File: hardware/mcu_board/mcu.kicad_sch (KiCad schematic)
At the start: 18 parts, among them J1 COLD, J1 TANK-BOTTOM, J1 TANK-TOP, J4 DISPLAY, J6 Conn_01x02_Pin, J7 RTC, SW1 RotaryEncoder_Switch, U1 ESP32-S3-DevKitC, U2 TOP, U3 BOTTOM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

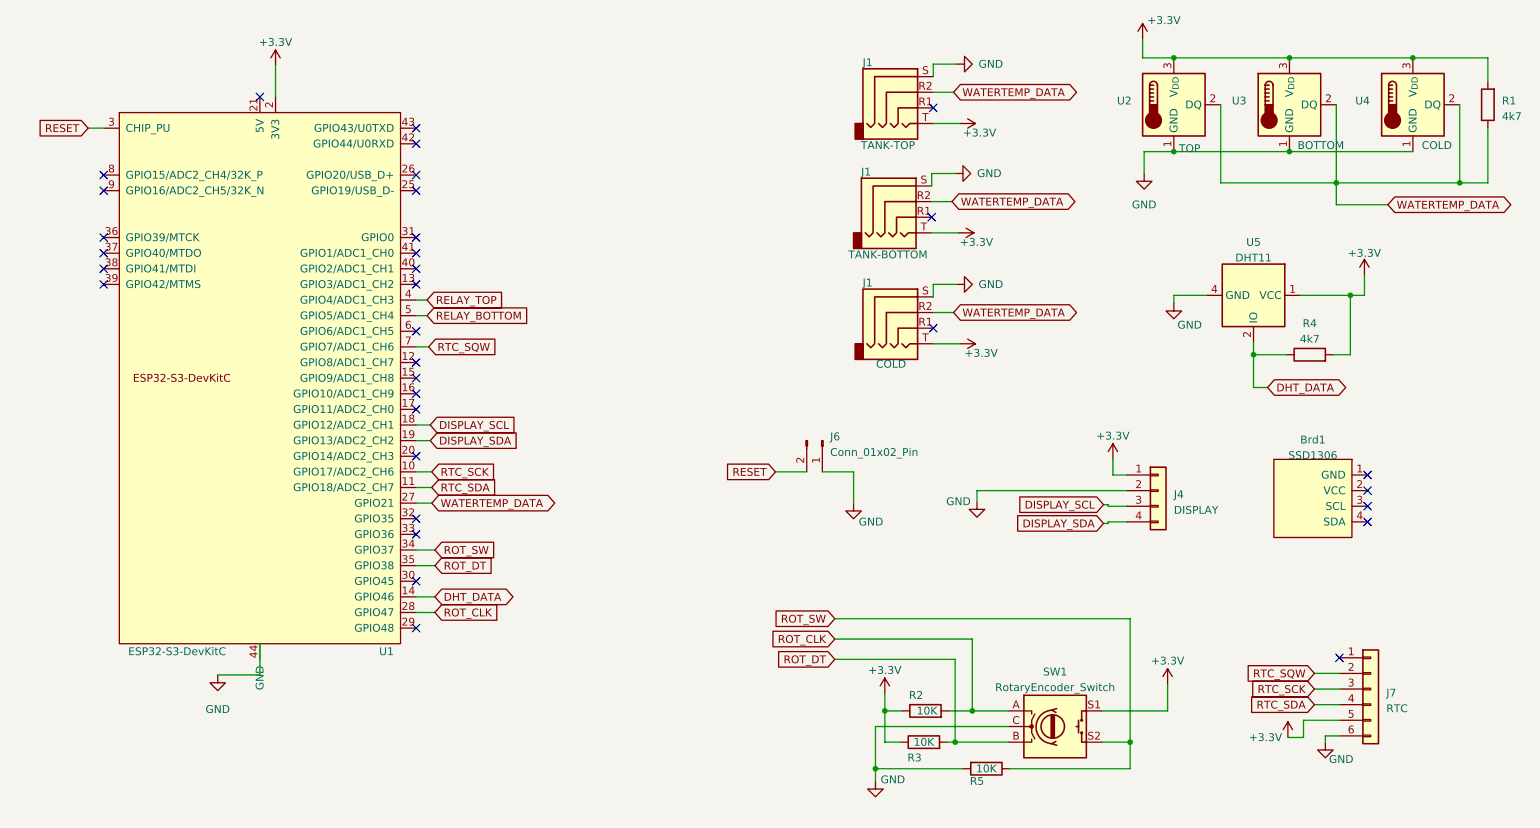
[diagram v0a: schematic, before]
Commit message: Refactored PCBs for v2. See README
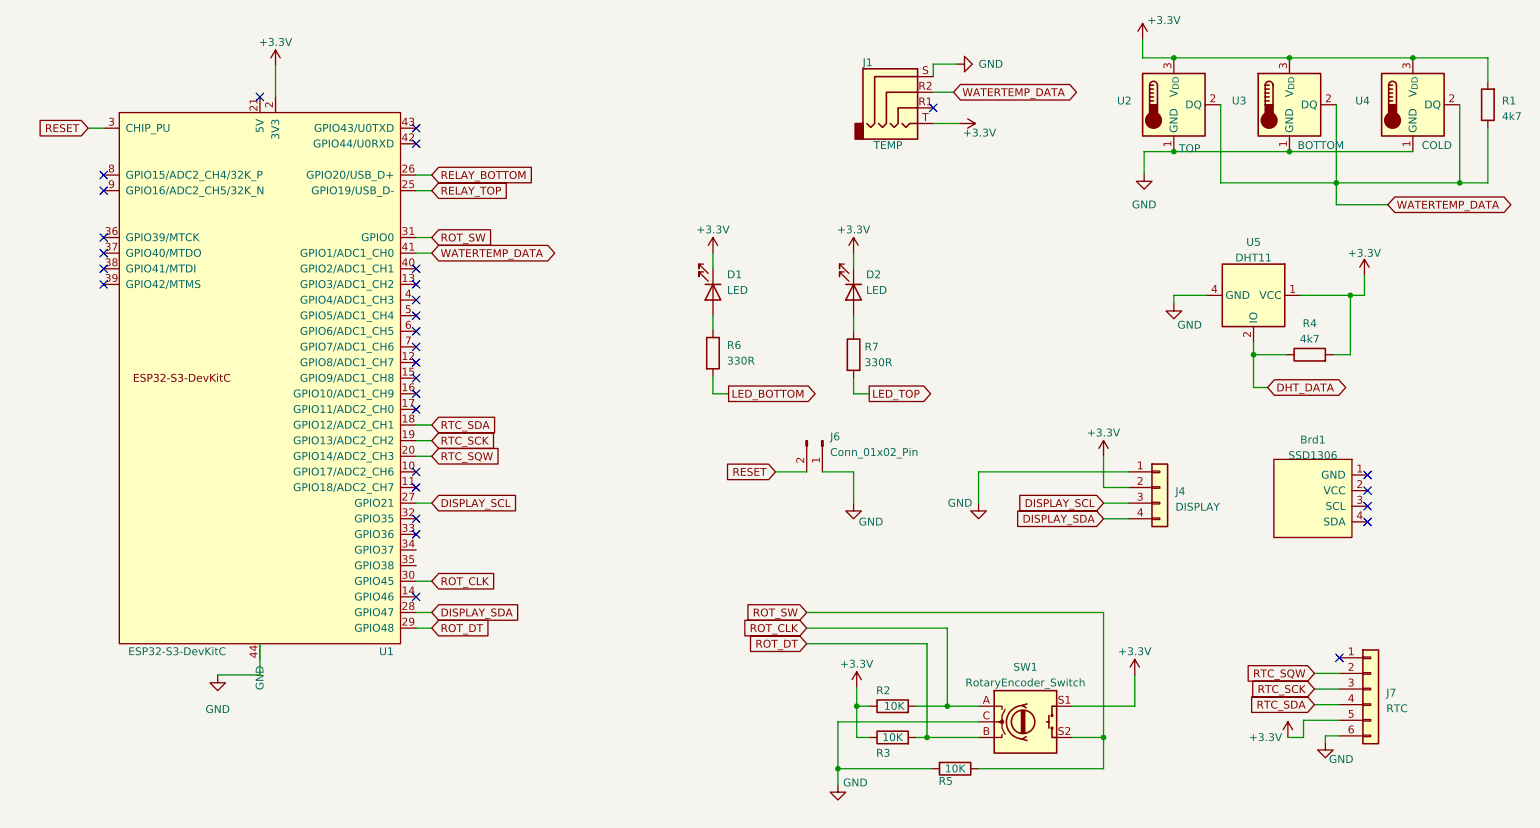
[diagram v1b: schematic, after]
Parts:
- removed J1: TANK-BOTTOM, Connector_Audio:Jack_3.5mm_PJ320D_Horizontal_NG, symbol Connector_Audio:AudioJack4
- removed J1: COLD, Connector_Audio:Jack_3.5mm_PJ320D_Horizontal_NG, symbol Connector_Audio:AudioJack4
- added D1, D2: LED, Diode_SMD:D_0805_2012Metric_Pad1.15x1.40mm_HandSolder, symbol Device:LED
- added R6, R7: 330R, Resistor_SMD:R_0805_2012Metric_Pad1.20x1.40mm_HandSolder, symbol Device:R
- J1: value TANK-TOP -> TEMP
- R4, U5: now left out of the parts list
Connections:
- net +3.3V: now also J4.2 (Pin_2), D1.1 (K), D2.1 (K); no longer J4.1 (Pin_1)
- net DHT_DATA: no longer U1.14 (GPIO46)
- net DISPLAY_SCL: now also U1.27 (GPIO21); no longer U1.18 (GPIO12/ADC2_CH1)
- net DISPLAY_SDA: now also U1.28 (GPIO47); no longer U1.19 (GPIO13/ADC2_CH2)
- net GND: now also J4.1 (Pin_1); no longer J4.2 (Pin_2)
- net RELAY_BOTTOM: now also U1.26 (GPIO20/USB_D+); no longer U1.5 (GPIO5/ADC1_CH4)
- net RELAY_TOP: now also U1.25 (GPIO19/USB_D-); no longer U1.4 (GPIO4/ADC1_CH3)
- net ROT_CLK: now also U1.30 (GPIO45); no longer U1.28 (GPIO47)
- net ROT_DT: now also U1.29 (GPIO48); no longer U1.35 (GPIO38)
- net ROT_SW: now also U1.31 (GPIO0); no longer U1.34 (GPIO37)
- net RTC_SCK: now also U1.19 (GPIO13/ADC2_CH2); no longer U1.10 (GPIO17/ADC2_CH6)
- net RTC_SDA: now also U1.18 (GPIO12/ADC2_CH1); no longer U1.11 (GPIO18/ADC2_CH7)
- net RTC_SQW: now also U1.20 (GPIO14/ADC2_CH3); no longer U1.7 (GPIO7/ADC1_CH6)
- net WATERTEMP_DATA: now also U1.41 (GPIO1/ADC1_CH0); no longer U1.27 (GPIO21)
- new net: D1.2 (A), R6.1
- new net: D2.2 (A), R7.1
- new net LED_BOTTOM: R6.2
- new net LED_TOP: R7.2
- no-connect marks 33 -> 30
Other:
- moved on the sheet: J4, R2, R3, R5, SW1

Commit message: v2 layout changes to fit in bax
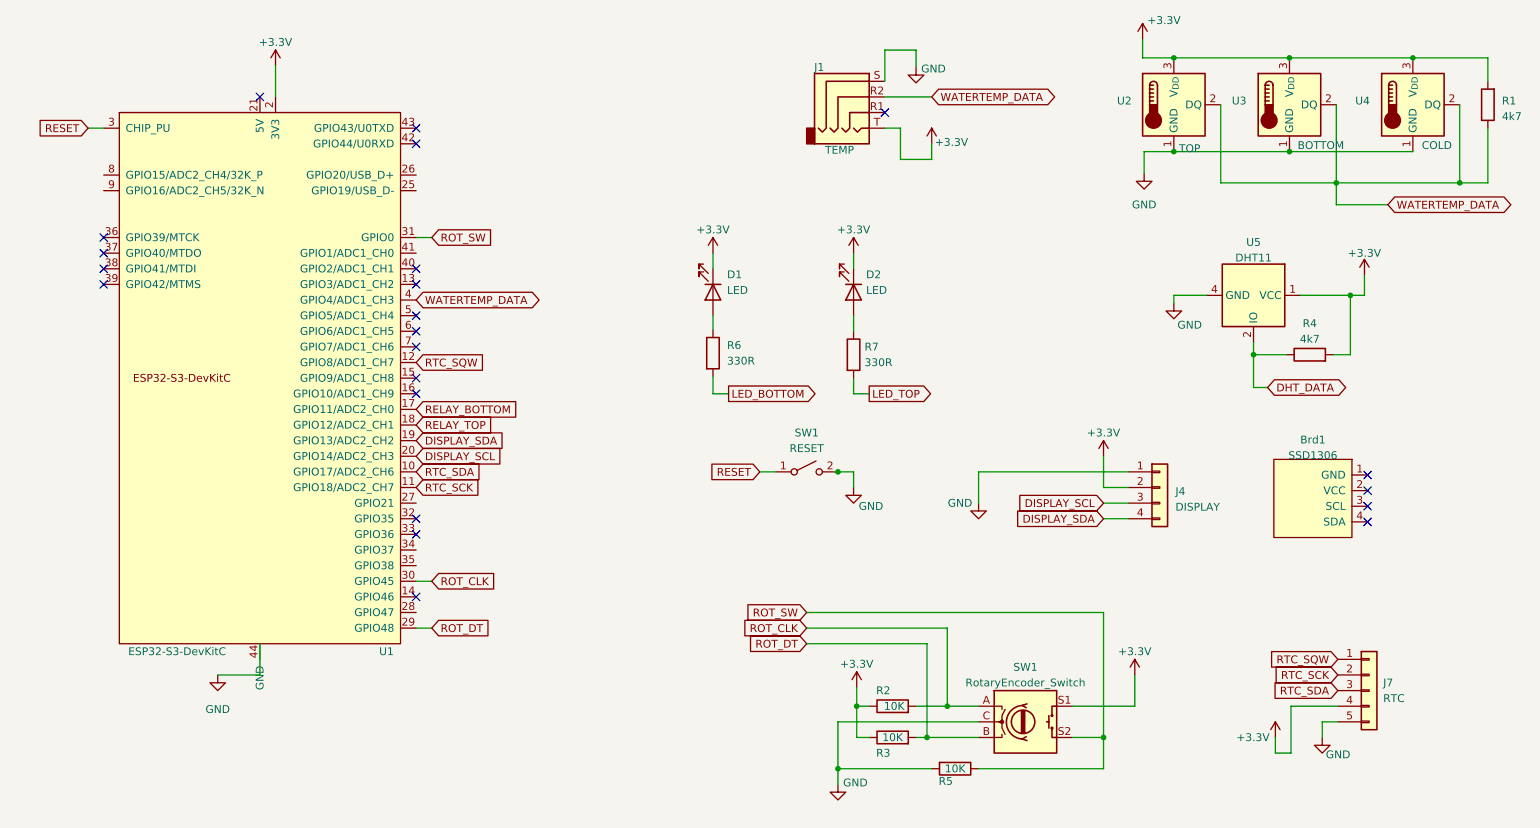
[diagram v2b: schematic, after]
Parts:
- removed J6: Conn_01x02_Pin, Connector_PinHeader_2.54mm:PinHeader_1x02_P2.54mm_Vertical, symbol Connector:Conn_01x02_Pin
- added SW1: RESET, Button_Switch_THT:SW_Tactile_SPST_Angled_PTS645Vx39-2LFS, symbol Switch:SW_SPST
- J7: footprint Connector_PinHeader_2.54mm:PinHeader_1x06_P2.54mm_Vertical -> Connector_PinHeader_2.54mm:PinHeader_1x05_P2.54mm_Vertical; symbol Connector_Generic:Conn_01x06 -> Connector_Generic:Conn_01x05
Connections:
- net +3.3V: now also J7.4 (Pin_4); no longer J7.5 (Pin_5)
- net DISPLAY_SCL: now also U1.20 (GPIO14/ADC2_CH3); no longer U1.27 (GPIO21)
- net DISPLAY_SDA: now also U1.19 (GPIO13/ADC2_CH2); no longer U1.28 (GPIO47)
- net GND: now also J7.5 (Pin_5), SW1.2 (B); no longer J7.6 (Pin_6)
- net RELAY_BOTTOM: now also U1.17 (GPIO11/ADC2_CH0); no longer U1.26 (GPIO20/USB_D+)
- net RELAY_TOP: now also U1.18 (GPIO12/ADC2_CH1); no longer U1.25 (GPIO19/USB_D-)
- net RESET: now also SW1.1 (A)
- net RTC_SCK: now also J7.2 (Pin_2), U1.11 (GPIO18/ADC2_CH7); no longer J7.3 (Pin_3), U1.19 (GPIO13/ADC2_CH2)
- net RTC_SDA: now also J7.3 (Pin_3), U1.10 (GPIO17/ADC2_CH6); no longer J7.4 (Pin_4), U1.18 (GPIO12/ADC2_CH1)
- net RTC_SQW: now also J7.1 (Pin_1), U1.12 (GPIO8/ADC1_CH7); no longer J7.2 (Pin_2), U1.20 (GPIO14/ADC2_CH3)
- net WATERTEMP_DATA: now also U1.4 (GPIO4/ADC1_CH3); no longer U1.41 (GPIO1/ADC1_CH0)
- no-connect marks 30 -> 22
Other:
- moved on the sheet: J1

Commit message: Laypout tweaks to fit case
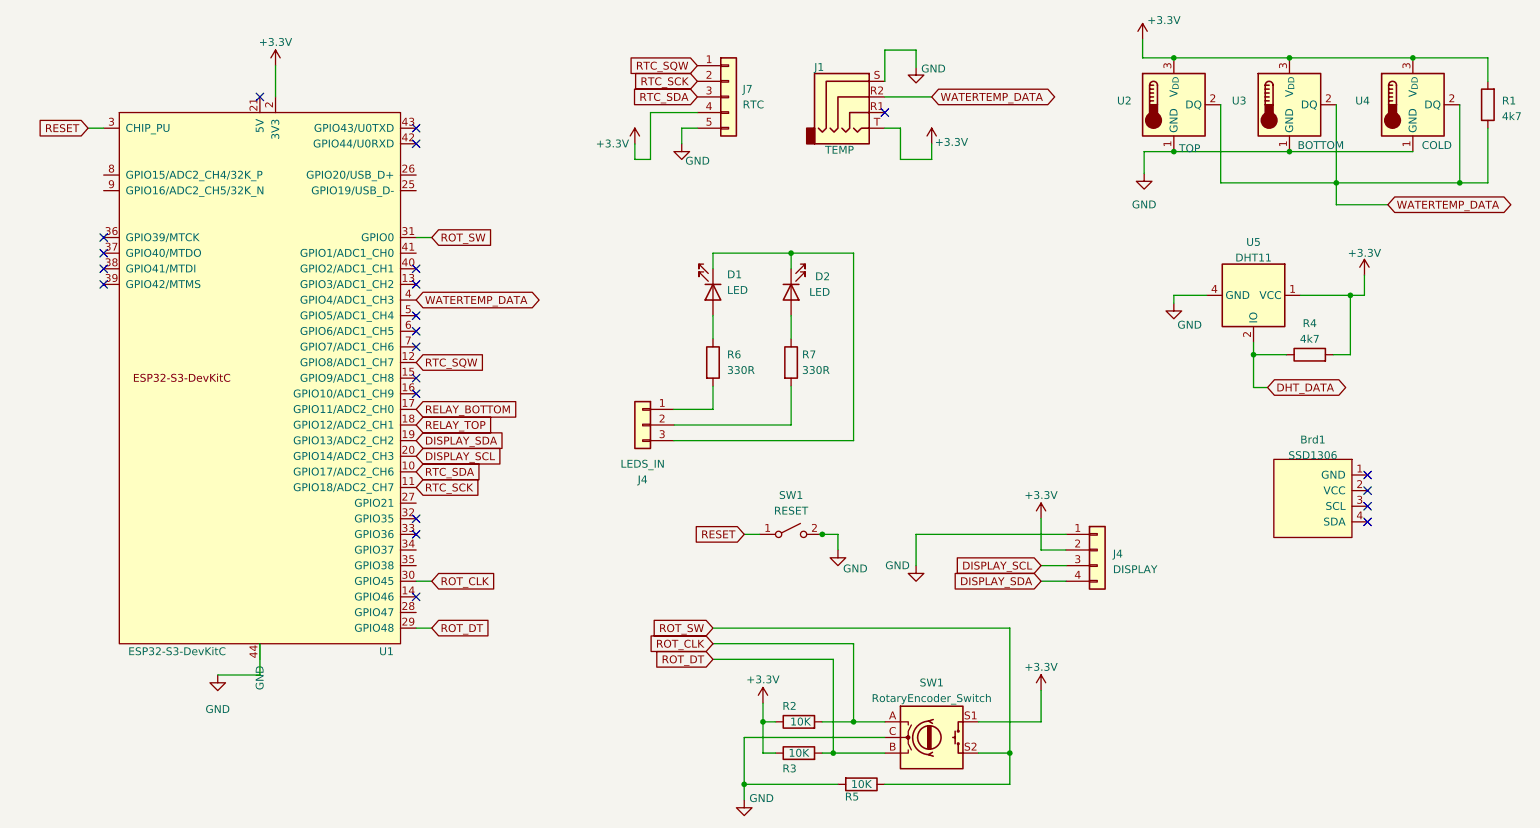
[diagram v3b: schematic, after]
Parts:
- added J4: LEDS_IN, Connector_PinHeader_2.54mm:PinHeader_1x03_P2.54mm_Vertical, symbol Connector_Generic:Conn_01x03
- J1: footprint Connector_Audio:Jack_3.5mm_PJ320D_Horizontal_NG -> Connector_Audio_2:Jack_3.5mm_PJ320D_Horizontal
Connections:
- net +3.3V: no longer D1.1 (K), D2.1 (K)
- net LED_BOTTOM: no longer names the net of R6.2
- net LED_BOTTOM: now also J4.1 (Pin_1)
- net LED_TOP: no longer names the net of R7.2
- net LED_TOP: now also J4.2 (Pin_2)
- new net: D1.1 (K), D2.1 (K), J4.3 (Pin_3)
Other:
- moved on the sheet: D2, J4, J7, R2, R3, R5, R6, R7, SW1
